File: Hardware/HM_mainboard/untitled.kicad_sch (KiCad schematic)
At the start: 14 parts, among them J1 JST PH2P ST90, Q1 PMOS - AS3401, U1 MCP73831-2, U2 TC1262-33

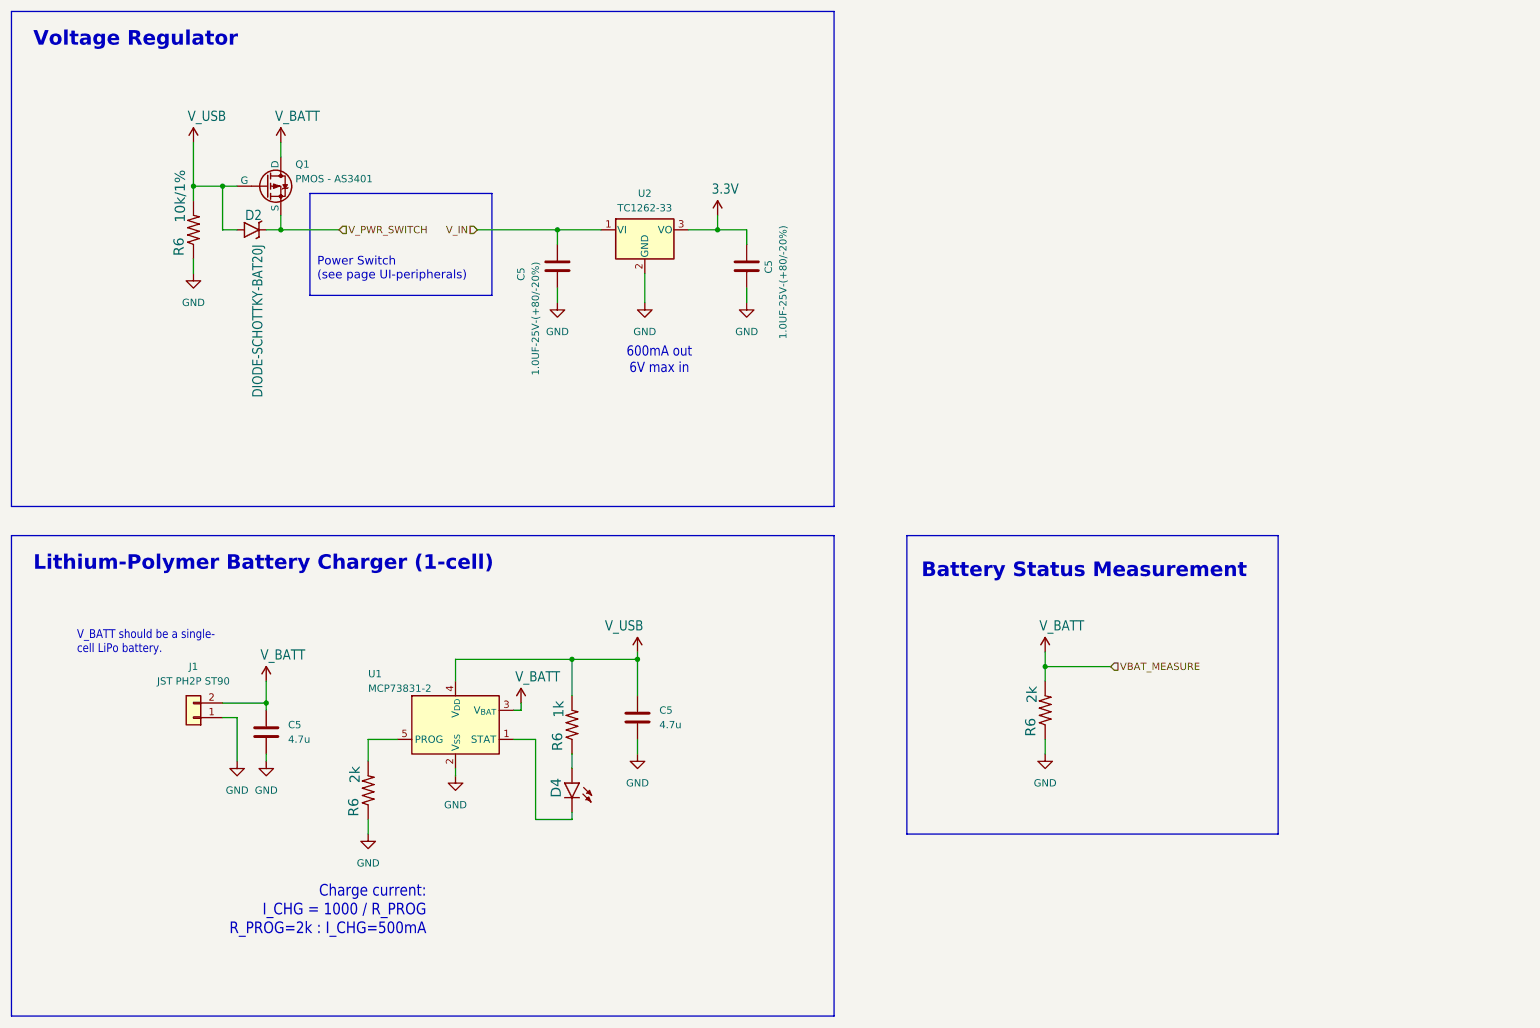
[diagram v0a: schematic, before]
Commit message: Added IMUs, updated some components
- Added 2 additonal IMUs:
     1) 6-Axis MC6470
     2) 9-Axis BNO55
- Replaced button jack connectors
- Replaced battery charging LED by a charging status measurement circuit
- Replaced caps for clock crystal
- Added stabalizing caps to uC Vcc
- Added UART pin header
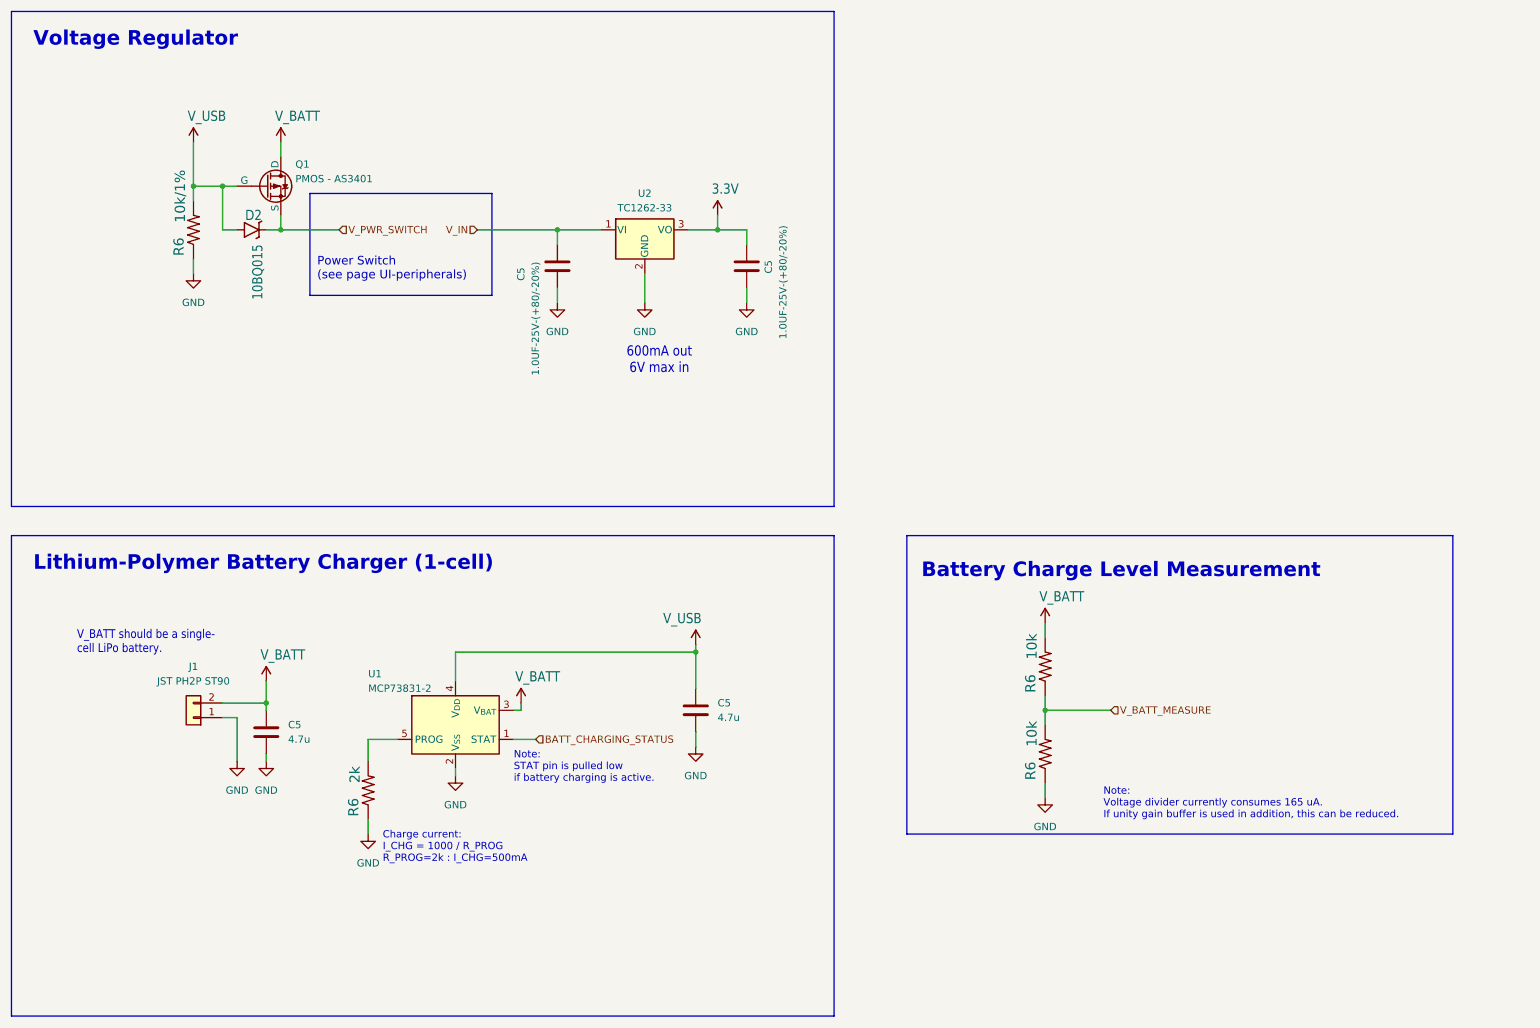
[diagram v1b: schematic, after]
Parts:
- removed D4: ~, esp32-thing:LED-0603, symbol esp32-thing-eagle-import:LED-YELLOW0603
- C5: footprint Capacitor_SMD:C_0201_0603Metric_Pad0.64x0.40mm_HandSolder -> Capacitor_SMD:C_0603_1608Metric_Pad1.08x0.95mm_HandSolder
- D2: value DIODE-SCHOTTKY-BAT20J -> 10BQ015; footprint esp32-thing:SOD-323 -> Diode_SMD:D_SMB_Handsoldering
- R6: footprint Resistor_SMD:R_0201_0603Metric_Pad0.64x0.40mm_HandSolder -> Resistor_SMD:R_0603_1608Metric_Pad0.98x0.95mm_HandSolder
- R6: value 1k -> 10k; footprint Resistor_SMD:R_0201_0603Metric_Pad0.64x0.40mm_HandSolder -> Resistor_SMD:R_0603_1608Metric_Pad0.98x0.95mm_HandSolder
- R6: value 2k -> 10k; footprint Resistor_SMD:R_0201_0603Metric_Pad0.64x0.40mm_HandSolder -> Resistor_SMD:R_0603_1608Metric_Pad0.98x0.95mm_HandSolder
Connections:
- net V_BATT: now also R6.2; no longer R6.2
- net V_USB: no longer R6.2
- net V_BATT_MEASURE: now reaches R6.1
- net V_BATT_MEASURE: now also R6.2
- net BATT_CHARGING_STATUS: now reaches U1.1 (STAT)
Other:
- note added: "Battery Charge Level Measurement"
- note added: "Note: STAT pin is pulled low if battery charging is active."
- note added: "Note: Voltage divider currently consumes 165 uA. If unity gain buffer is used in addition, this can be reduced."
- note removed: "Battery Status Measurement"
- moved on the sheet: C5, R6

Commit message: Changed I2C address selection of IMUs
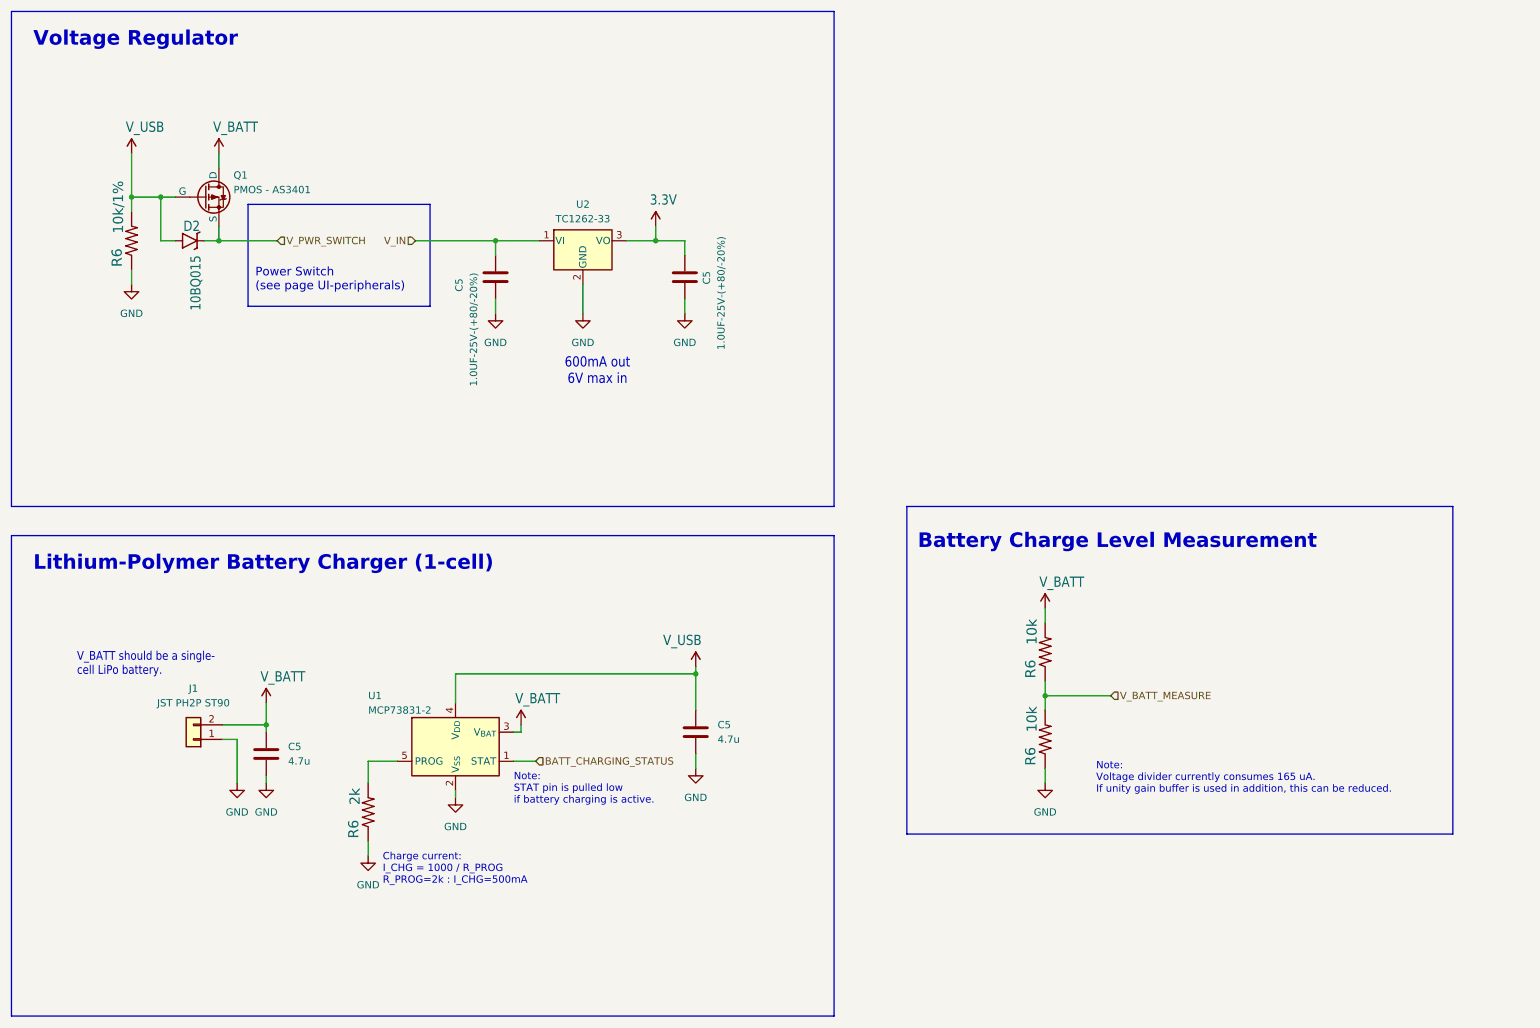
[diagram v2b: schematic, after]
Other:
- moved on the sheet: C5, D2, J1, Q1, R6, U1, U2

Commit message: Started component placement for PCB
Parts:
- U1: footprint Package_TO_SOT_SMD:SOT-23-5 -> Package_TO_SOT_SMD:SOT-23-5_HandSoldering
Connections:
- net V_PWR_SWITCH: now also D2.1 (C); no longer D2.C
- net V_USB: now also D2.2 (A); no longer D2.A
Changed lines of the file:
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@@
         )
         (path "/54a6df43-5475-46a2-9916-8b0260700d4c/b19d5209-4861-4a96-a3d1-daca4a23de52"
-          (reference "C4") (unit 1)
+          (reference "C3") (unit 1)
         )
       )
@@
         )
         (path "/54a6df43-5475-46a2-9916-8b0260700d4c/b19d5209-4861-4a96-a3d1-daca4a23de52"
-          (reference "#SUPPLY06") (unit 1)
+          (reference "#SUPPLY05") (unit 1)
         )
       )
@@
         )
         (path "/54a6df43-5475-46a2-9916-8b0260700d4c/b19d5209-4861-4a96-a3d1-daca4a23de52"
-          (reference "#PWR09") (unit 1)
+          (reference "#PWR08") (unit 1)
         )
       )
@@
         )
         (path "/54a6df43-5475-46a2-9916-8b0260700d4c/b19d5209-4861-4a96-a3d1-daca4a23de52"
-          (reference "R7") (unit 1)
+          (reference "R3") (unit 1)
         )
       )
@@
         )
         (path "/54a6df43-5475-46a2-9916-8b0260700d4c/b19d5209-4861-4a96-a3d1-daca4a23de52"
-          (reference "#SUPPLY05") (unit 1)
+          (reference "#SUPPLY06") (unit 1)
         )
       )
@@
         )
         (path "/54a6df43-5475-46a2-9916-8b0260700d4c/b19d5209-4861-4a96-a3d1-daca4a23de52"
+          (reference "#PWR09") (unit 1)
+        )
+      )
+    )
+  )
+  (symbol (lib_name "GND_1") (lib_id "power:GND") (at 120.015 71.755 0) (unit 1)
+    (in_bom yes) (on_board yes) (dnp no) (fields_autoplaced)
+    (property "Reference" "#PWR06" (at 120.015 78.105 0)
+      (effects (font (size 1.27 1.27)) hide)
+    )
+    (property "Value" "GND" (at 120.015 76.835 0)
+      (effects (font (size 1.27 1.27)))
+    )
+    (property "Footprint" "" (at 120.015 71.755 0)
+      (effects (font (size 1.27 1.27)) hide)
+    )
+    (property "Datasheet" "" (at 120.015 71.755 0)
+      (effects (font (size 1.27 1.27)) hide)
+    )
+    (pin "1")
+    (instances
+      (project "HM_mainboard"
+        (path "/54a6df43-5475-46a2-9916-8b0260700d4c"
+          (reference "#PWR06") (unit 1)
+        )
+        (path "/54a6df43-5475-46a2-9916-8b0260700d4c/8a725ce3-408a-4762-9df2-b56094186e56"
+          (reference "#PWR016") (unit 1)
+        )
+        (path "/54a6df43-5475-46a2-9916-8b0260700d4c/9043a365-e24a-41b8-9f6d-decb4da0da6a"
+          (reference "#PWR010") (unit 1)
+        )
+        (path "/54a6df43-5475-46a2-9916-8b0260700d4c/137c5701-d01e-40ce-919d-b371cfda41da"
+          (reference "#PWR01") (unit 1)
+        )
+        (path "/54a6df43-5475-46a2-9916-8b0260700d4c/b19d5209-4861-4a96-a3d1-daca4a23de52"
           (reference "#PWR07") (unit 1)
-        )
-      )
-    )
-  )
-  (symbol (lib_name "GND_1") (lib_id "power:GND") (at 120.015 71.755 0) (unit 1)
-    (in_bom yes) (on_board yes) (dnp no) (fields_autoplaced)
-    (property "Reference" "#PWR06" (at 120.015 78.105 0)
-      (effects (font (size 1.27 1.27)) hide)
-    )
-    (property "Value" "GND" (at 120.015 76.835 0)
-      (effects (font (size 1.27 1.27)))
-    )
-    (property "Footprint" "" (at 120.015 71.755 0)
-      (effects (font (size 1.27 1.27)) hide)
-    )
-    (property "Datasheet" "" (at 120.015 71.755 0)
-      (effects (font (size 1.27 1.27)) hide)
-    )
-    (pin "1")
-    (instances
-      (project "HM_mainboard"
-        (path "/54a6df43-5475-46a2-9916-8b0260700d4c"
-          (reference "#PWR06") (unit 1)
-        )
-        (path "/54a6df43-5475-46a2-9916-8b0260700d4c/8a725ce3-408a-4762-9df2-b56094186e56"
-          (reference "#PWR016") (unit 1)
-        )
-        (path "/54a6df43-5475-46a2-9916-8b0260700d4c/9043a365-e24a-41b8-9f6d-decb4da0da6a"
-          (reference "#PWR010") (unit 1)
-        )
-        (path "/54a6df43-5475-46a2-9916-8b0260700d4c/137c5701-d01e-40ce-919d-b371cfda41da"
-          (reference "#PWR01") (unit 1)
-        )
-        (path "/54a6df43-5475-46a2-9916-8b0260700d4c/b19d5209-4861-4a96-a3d1-daca4a23de52"
-          (reference "#PWR08") (unit 1)
         )
       )
@@
       (effects (font (size 1.27 1.27)) (justify left))
     )
-    (property "Footprint" "Package_TO_SOT_SMD:SOT-23-5" (at 99.06 153.67 0)
+    (property "Footprint" "Package_TO_SOT_SMD:SOT-23-5_HandSoldering" (at 99.06 153.67 0)
       (effects (font (size 1.27 1.27) italic) (justify left) hide)
     )
@@
         )
         (path "/54a6df43-5475-46a2-9916-8b0260700d4c/b19d5209-4861-4a96-a3d1-daca4a23de52"
-          (reference "C3") (unit 1)
+          (reference "C4") (unit 1)
         )
       )
@@
         )
         (path "/54a6df43-5475-46a2-9916-8b0260700d4c/b19d5209-4861-4a96-a3d1-daca4a23de52"
-          (reference "#SUPPLY03") (unit 1)
+          (reference "#SUPPLY02") (unit 1)
         )
       )
@@
         )
         (path "/54a6df43-5475-46a2-9916-8b0260700d4c/b19d5209-4861-4a96-a3d1-daca4a23de52"
-          (reference "#SUPPLY02") (unit 1)
+          (reference "#SUPPLY03") (unit 1)
         )
       )
@@
       (effects (font (size 1.778 1.5113)) (justify right top))
     )
-    (property "Footprint" "Diode_SMD:D_SMB_Handsoldering" (at 51.435 59.055 0)
+    (property "Footprint" "Diode_SMD:D_SMB_Handsoldering" (at 51.435 62.865 0)
       (effects (font (size 1.27 1.27)) hide)
     )
@@
       (effects (font (size 1.27 1.27)) hide)
     )
-    (pin "A")
-    (pin "C")
-    (instances
-      (project "HM_mainboard"
+    (pin "2")
+    (pin "1")
+    (instances
+      (project "HM_mainboard"
